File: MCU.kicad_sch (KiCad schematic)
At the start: 19 parts, among them U1 113991054, U2 SN74LVC2G17DBVR

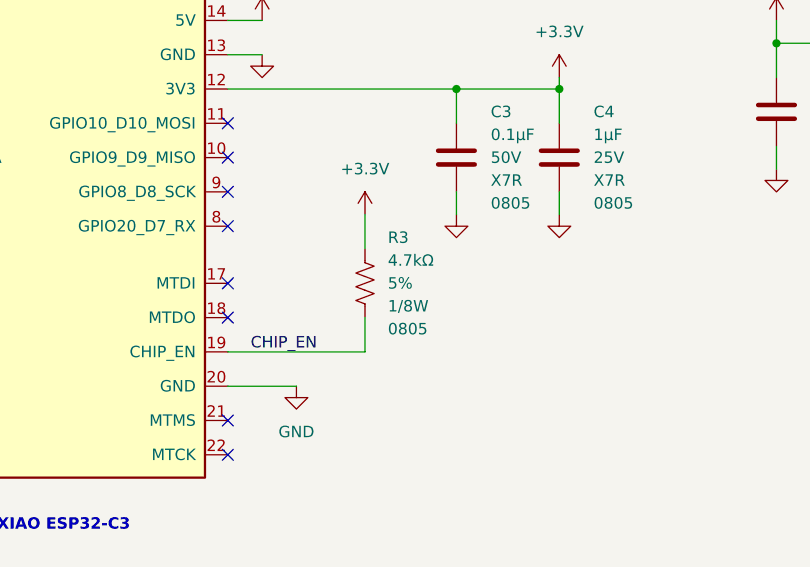
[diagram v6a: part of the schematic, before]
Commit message: removed duplicated pullup resistor on chip en
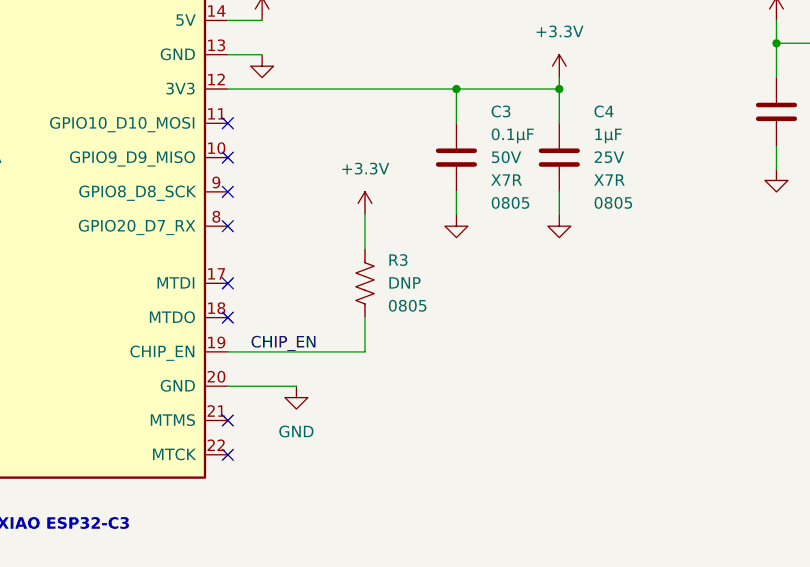
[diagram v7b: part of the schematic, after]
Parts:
- removed R3: RMCF0805JT4K70, Resistor_SMD:R_0805_2012Metric_Pad1.20x1.40mm_HandSolder, symbol Resistors:RMCF0805JT4K70
- added R3: DNP 0805, Resistor_SMD:R_0805_2012Metric_Pad1.20x1.40mm_HandSolder, symbol Resistors:DNP_0805
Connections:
- net +3.3V: now also R3.2
- net CHIP_EN: now also R3.1
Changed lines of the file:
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@@
+	(symbol
+		(lib_id "Resistors:DNP_0805")
+		(at 171.45 76.2 180)
+		(unit 1)
+		(exclude_from_sim no)
+		(in_bom yes)
+		(on_board yes)
+		(dnp no)
+		(fields_autoplaced yes)
+		(property "Reference" "R3"
+			(at 173.99 73.6599 0)
+			(effects
+				(font
+					(size 1.27 1.27)
+				)
+				(justify right)
+			)
+		)
+		(property "Value" "DNP 0805"
+			(at 168.148 61.976 0)
+			(effects
+				(font
+					(size 1.27 1.27)
+				)
+				(justify left bottom)
+				(hide yes)
+			)
+		)
+		(property "Footprint" "Resistor_SMD:R_0805_2012Metric_Pad1.20x1.40mm_HandSolder"
+			(at 170.434 54.61 0)
+			(effects
+				(font
+					(size 1.27 1.27)
+				)
+				(justify bottom)
+				(hide yes)
+			)
+		)
+		(property "Datasheet" ""
+			(at 171.45 76.2 90)
+			(effects
+				(font
+					(size 1.27 1.27)
+				)
+				(hide yes)
+			)
+		)
+		(property "Description" "Res 0805 Do Not Populate"
+			(at 170.688 57.404 0)
+			(effects
+				(font
+					(size 1.27 1.27)
+				)
+				(hide yes)
+			)
+		)
+		(property "PARTREV" "V.12"
+			(at 162.56 52.07 0)
+			(effects
+				(font
+					(size 1.27 1.27)
+				)
+				(justify bottom)
+				(hide yes)
+			)
+		)
+		(property "STANDARD" "IPC 7351B"
+			(at 170.942 52.07 0)
+			(effects
+				(font
+					(size 1.27 1.27)
+				)
+				(justify bottom)
+				(hide yes)
+			)
+		)
+		(property "MAXIMUM_PACKAGE_HEIGHT" "0.6 mm"
+			(at 180.848 52.07 0)
+			(effects
+				(font
+					(size 1.27 1.27)
+				)
+				(justify bottom)
+				(hide yes)
+			)
+		)
+		(property "MANUFACTURER" "Yageo"
+			(at 171.196 58.42 0)
+			(effects
+				(font
+					(size 1.27 1.27)
+				)
+				(justify bottom)
+				(hide yes)
+			)
+		)
+		(property "Resistance" "DNP"
+			(at 173.99 76.1999 0)
+			(effects
+				(font
+					(size 1.27 1.27)
+				)
+				(justify right)
+			)
+		)
+		(property "Tolerance" "-"
+			(at 171.45 50.038 0)
+			(effects
+				(font
+					(size 1.27 1.27)
+				)
+				(justify left)
+				(hide yes)
+			)
+		)
+		(property "Power" "1/8W"
+			(at 171.704 51.054 0)
+			(effects
+				(font
+					(size 1.27 1.27)
+				)
+				(justify left)
+				(hide yes)
+			)
+		)
+		(property "Package" "0805"
+			(at 173.99 78.7399 0)
+			(effects
+				(font
+					(size 1.27 1.27)
+				)
+				(justify right)
+			)
+		)
+		(pin "2"
+		)
+		(pin "1"
+		)
+		(instances
+			(project "EauRouge"
+				(path "/c4971751-18ba-42c0-933f-7e935423e3d9/c917e16d-f0ac-4e75-a6ca-53a802df9d55"
+					(reference "R3")
+					(unit 1)
+				)
+			)
+		)
+	)
 	(symbol
 		(lib_id "Resistors:DNP_0805")
@@
 					(unit 1)
 				)
-			)
-		)
-	)
-	(symbol
-		(lib_id "Resistors:RMCF0805JT4K70")
-		(at 171.45 76.2 0)
-		(unit 1)
-		(exclude_from_sim no)
-		(in_bom yes)
-		(on_board yes)
-		(dnp no)
-		(fields_autoplaced yes)
-		(property "Reference" "R3"
-			(at 173.99 71.1199 0)
-			(effects
-				(font
-					(size 1.27 1.27)
-				)
-				(justify left)
-			)
-		)
-		(property "Value" "RMCF0805JT4K70"
-			(at 183.388 102.108 0)
-			(effects
-				(font
-					(size 1.27 1.27)
-				)
-				(justify left bottom)
-				(hide yes)
-			)
-		)
-		(property "Footprint" "Resistor_SMD:R_0805_2012Metric_Pad1.20x1.40mm_HandSolder"
-			(at 172.466 97.79 0)
-			(effects
-				(font
-					(size 1.27 1.27)
-				)
-				(justify bottom)
-				(hide yes)
-			)
-		)
-		(property "Datasheet" ""
-			(at 171.45 76.2 90)
-			(effects
-				(font
-					(size 1.27 1.27)
-				)
-				(hide yes)
-			)
-		)
-		(property "Description" "RES 4.7K OHM 5% 1/8W 0805"
-			(at 172.212 94.996 0)
-			(effects
-				(font
-					(size 1.27 1.27)
-				)
-				(hide yes)
-			)
-		)
-		(property "PARTREV" "V.12"
-			(at 180.34 100.33 0)
-			(effects
-				(font
-					(size 1.27 1.27)
-				)
-				(justify bottom)
-				(hide yes)
-			)
-		)
-		(property "STANDARD" "IPC 7351B"
-			(at 171.958 100.33 0)
-			(effects
-				(font
-					(size 1.27 1.27)
-				)
-				(justify bottom)
-				(hide yes)
-			)
-		)
-		(property "MAXIMUM_PACKAGE_HEIGHT" "0.6 mm"
-			(at 162.052 100.33 0)
-			(effects
-				(font
-					(size 1.27 1.27)
-				)
-				(justify bottom)
-				(hide yes)
-			)
-		)
-		(property "MANUFACTURER" "Yageo"
-			(at 171.704 93.98 0)
-			(effects
-				(font
-					(size 1.27 1.27)
-				)
-				(justify bottom)
-				(hide yes)
-			)
-		)
-		(property "Resistance" "4.7kΩ"
-			(at 173.99 73.6599 0)
-			(effects
-				(font
-					(size 1.27 1.27)
-				)
-				(justify left)
-			)
-		)
-		(property "Tolerance" "5%"
-			(at 173.99 76.1999 0)
-			(effects
-				(font
-					(size 1.27 1.27)
-				)
-				(justify left)
-			)
-		)
-		(property "Power" "1/8W"
-			(at 173.99 78.7399 0)
-			(effects
-				(font
-					(size 1.27 1.27)
-				)
-				(justify left)
-			)
-		)
-		(property "Package" "0805"
-			(at 173.99 81.2799 0)
-			(effects
-				(font
-					(size 1.27 1.27)
-				)
-				(justify left)
-			)
-		)
-		(pin "2"
-		)
-		(pin "1"
-		)
-		(instances
-			(project "Spa-Eau_Rouge"
-				(path "/c4971751-18ba-42c0-933f-7e935423e3d9/c917e16d-f0ac-4e75-a6ca-53a802df9d55"
-					(reference "R3")
-					(unit 1)
-				)

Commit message: ordered PCB
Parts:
- R11, R3, R4, R6, R8, R9: now not fitted
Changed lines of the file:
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@@
 		(in_bom yes)
 		(on_board yes)
-		(dnp no)
+		(dnp yes)
 		(fields_autoplaced yes)
 		(property "Reference" "R3"
@@
 		(in_bom yes)
 		(on_board yes)
-		(dnp no)
+		(dnp yes)
 		(property "Reference" "R8"
 			(at 154.178 141.478 90)
@@
 		(in_bom yes)
 		(on_board yes)
-		(dnp no)
+		(dnp yes)
 		(property "Reference" "R4"
 			(at 195.58 119.3799 0)
@@
 		(in_bom yes)
 		(on_board yes)
-		(dnp no)
+		(dnp yes)
 		(property "Reference" "R11"
 			(at 154.178 160.528 90)
@@
 		(in_bom yes)
 		(on_board yes)
-		(dnp no)
+		(dnp yes)
 		(fields_autoplaced yes)
 		(property "Reference" "R6"
@@
 		(in_bom yes)
 		(on_board yes)
-		(dnp no)
+		(dnp yes)
 		(fields_autoplaced yes)
 		(property "Reference" "R9"
